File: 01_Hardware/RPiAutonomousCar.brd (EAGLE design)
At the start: 67.3 x 34 mm, 37 parts, among them U1 TXB0108PWR, U4 MCP3004-I/ST

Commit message: ready for review
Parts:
- removed JP4, JP5: (no value), jumper:JP2
- added JP14, JP3: (no value), jumper:JP1
- moved LED1 2.17 mm to (61.7, 23.1)
- moved R1 1.80 mm to (61.7, 20.3)
- moved JP11 1.30 mm to (65.0, 10.2)
- moved JP7 0.36 mm to (3.05, 9.91)
- moved JP10 0.25 mm to (65.0, 3.81)
- moved JP2 0.25 mm to (34.0, 23.4)
- moved JP6 0.25 mm to (41.1, 6.10)
- moved U$1 0.25 mm to (56.6, 12.4)
- moved C8 0.25 mm to (28.7, 6.10)
- moved JP13 0.25 mm to (22.4, 6.10)
- moved JP9 0.25 mm to (17.8, 7.11)
- moved R3 0.25 mm to (25.1, 10.4)
- moved R4 0.25 mm to (26.7, 10.4)
- moved R5 0.25 mm to (27.9, 14.0)
- moved R8 0.25 mm to (25.7, 6.10)
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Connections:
- net +5V: now also JP14.2; no longer JP5.2
- net +UB: now also JP3.2; no longer JP4.2
- net GND: now also JP14.1, JP3.1; no longer JP4.1, JP4.3, JP5.1, JP5.3
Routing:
- net +5V: track 86.6 -> 77.4 mm
- net +UB: track 45.8 -> 50.9 mm
- net RPI3: track 19.5 -> 21.2 mm
- net RPI40: track 13.1 -> 11.6 mm
- net RPI5: track 19.0 -> 20.4 mm
- net M2_OUT1: track 9.27 -> 8.00 mm
- net M1_OUT2: track 9.80 -> 10.5 mm
- net M2_OUT2: track 8.83 -> 8.15 mm
- net N$12: track 1.85 -> 1.19 mm
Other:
- board text added: "+5V"
- board text added: "1"
- board text added: "FullStackEmbedded 2017/v1"
- board text added: "M1"
- board text added: "M2"
- board text added: "Vbat"

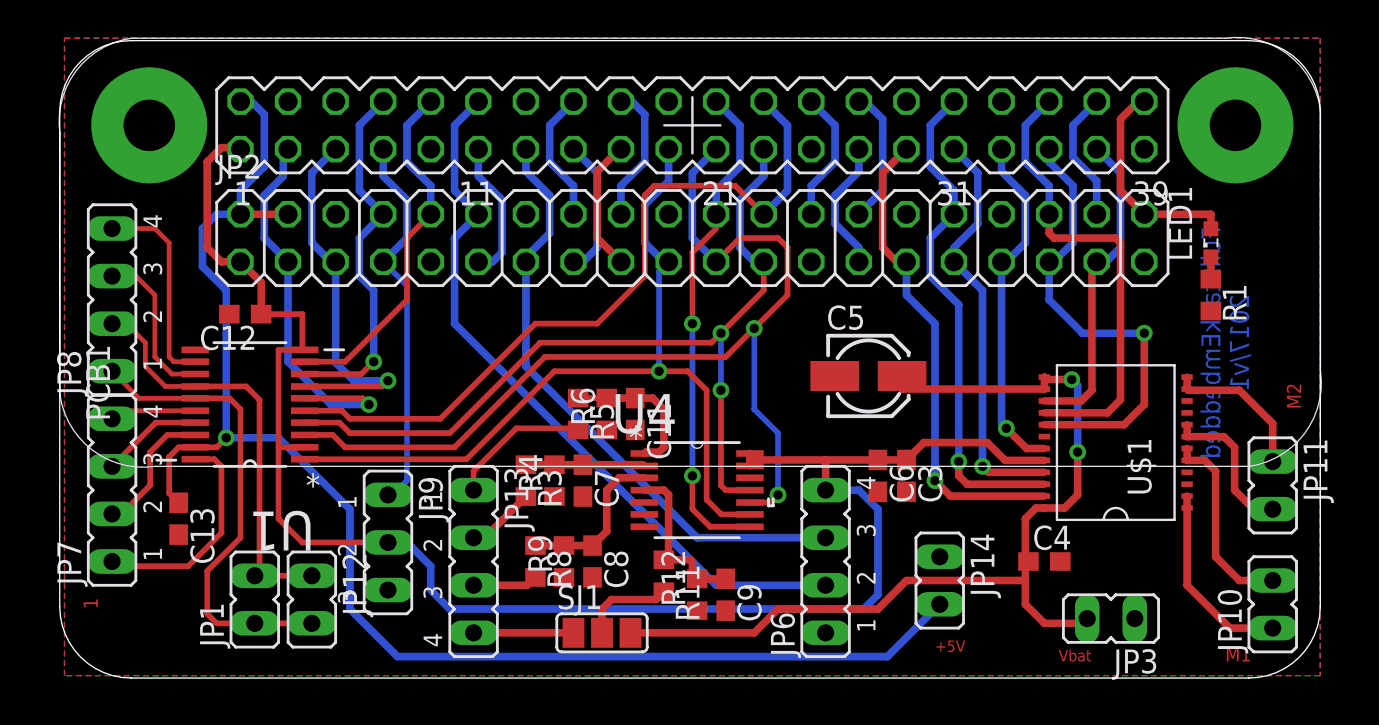
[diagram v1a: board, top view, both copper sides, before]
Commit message: routing done. Ready to order
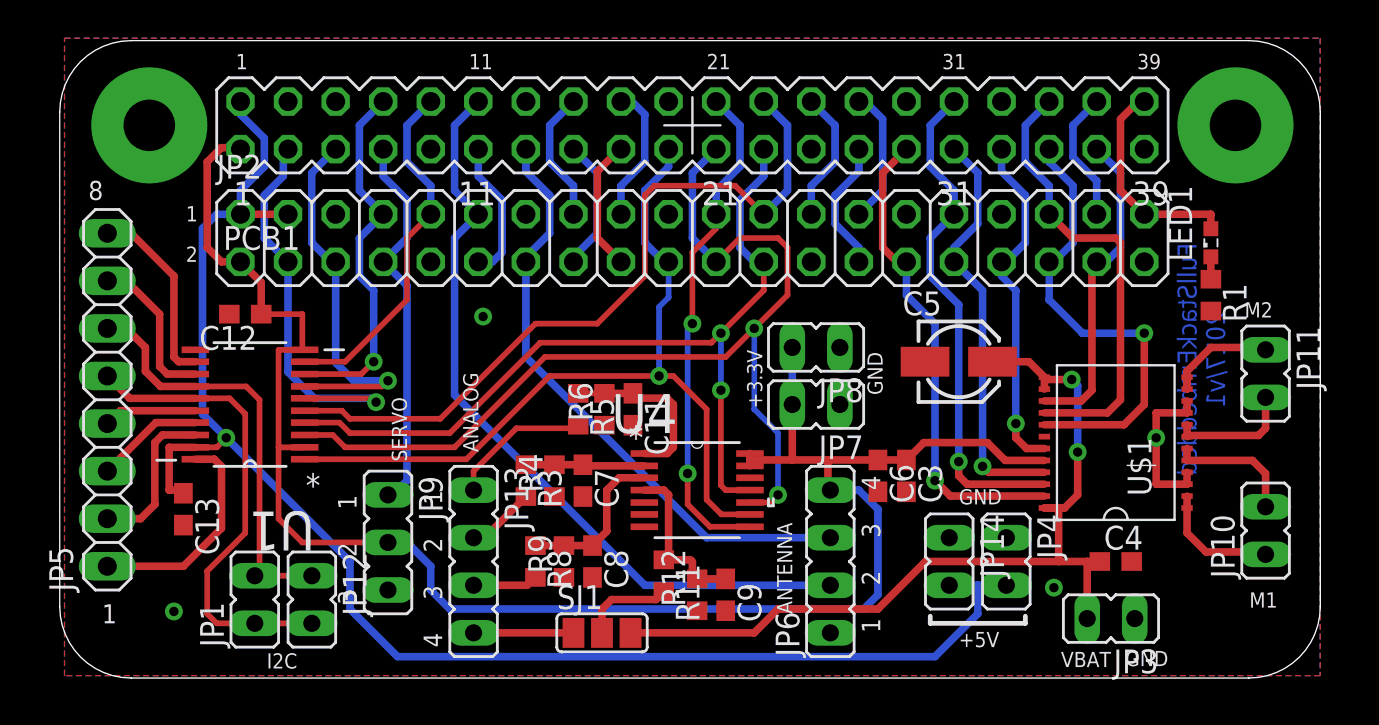
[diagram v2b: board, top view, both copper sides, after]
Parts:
- added JP4: (no value), jumper:JP1
- added JP5: (no value), pinhead:1X08
- JP7, JP8: device jumper:JP4 -> jumper:JP1
- R1: value 1K -> x
- moved JP7 37.9 mm to (40.6, 14.5)
- moved JP8 37.7 mm to (40.6, 17.5)
- moved JP11 5.98 mm to (64.6, 16.1)
- moved C5 4.89 mm to (48.3, 16.8)
- moved JP10 3.96 mm to (64.6, 7.75)
- moved C4 3.81 mm to (56.6, 6.10)
- moved JP14 1.14 mm to (47.8, 6.10)
- moved C13 0.57 mm to (6.86, 8.89)
- moved C11 0.28 mm to (30.9, 14.2)
- moved R6 0.28 mm to (29.3, 14.2)
- moved R5 0.25 mm to (27.9, 14.2)
- moved JP6 0.25 mm to (41.4, 6.10)
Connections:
- net +3V3: now also JP7.2, JP8.2
- net +5V: now also JP4.2
- net GND: now also JP4.1, JP7.1, JP8.1
- net N$1: now also JP5.8; no longer JP8.4
- net N$18: now also JP5.5; no longer JP8.1
- net N$2: now also JP5.7; no longer JP8.3
- net N$4: now also JP5.6; no longer JP8.2
- net N$5: now also JP5.4; no longer JP7.4
- net N$6: now also JP5.3; no longer JP7.3
- net N$7: now also JP5.2; no longer JP7.2
- net N$8: now also JP5.1; no longer JP7.1
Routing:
- net GND: track 0.00 -> 8.38 mm, vias 0 -> 4
- net +3V3: track 98.0 -> 103.9 mm
- net +5V: track 77.4 -> 82.1 mm
- net +UB: track 50.9 -> 46.9 mm
- net M1_OUT2: track 10.5 -> 6.89 mm
- net M1_OUT1: track 10.3 -> 6.63 mm
- net RPI12: track 39.0 -> 41.5 mm
- net M2_OUT1: track 8.00 -> 6.36 mm
- net M2_OUT2: track 8.15 -> 6.63 mm
- net N$11: track 8.03 -> 9.30 mm
- net N$7: track 7.23 -> 8.48 mm
- net RPI3: track 21.2 -> 22.2 mm
- net N$1: track 11.0 -> 10.1 mm
- net RPI36: track 24.8 -> 24.2 mm
- net RPI19: track 45.6 -> 45.0 mm
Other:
- board text added: "+3.3V"
- board text added: "11"
- board text added: "2"
- board text added: "21"
- board text added: "31"
- board text added: "39"
- board text added: "8"
- board text added: "ANALOG"
- board text added: "ANTENNA"
- board text added: "GND"
- board text added: "I2C"
- board text added: "SERVO"
- board text added: "VBAT"
- board text removed: "Vbat"
